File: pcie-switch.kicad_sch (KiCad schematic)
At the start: 130 parts, among them J5 Tag-Connect_TC2050-IDC-NL_2x5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, Q1 BSS138PW,115, Q2 BSS138PW,115, Q3 BSS138PW,115, Q4 BSS138PW,115, Q5 BSS138PW,115, U4 PI7C9X3G606GP, U5 NTS0302JKZ, U6 93AA66C_SOIC

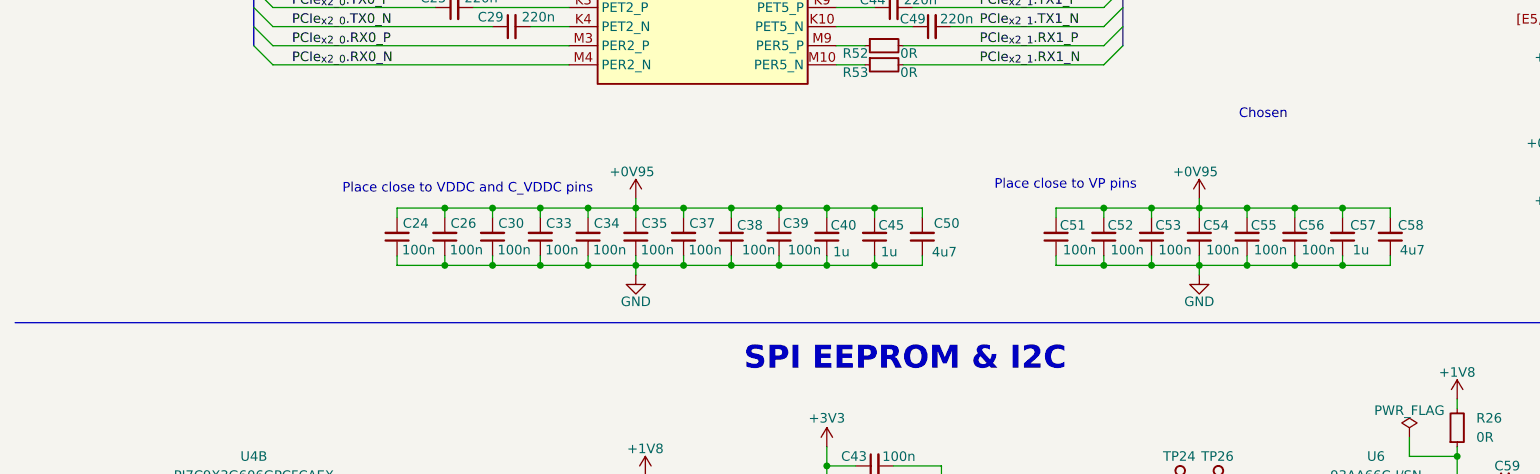
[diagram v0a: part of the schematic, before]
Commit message: [#101557] Add decoupling caps on VDDR, C_VDDR and VPH
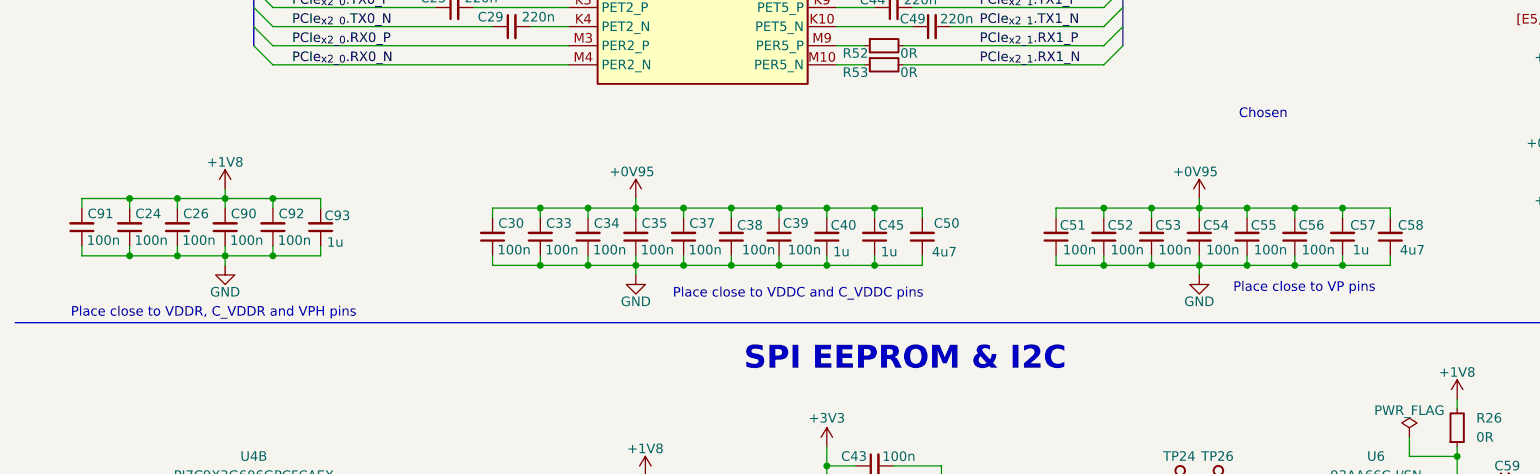
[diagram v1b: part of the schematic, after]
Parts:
- added C90, C91, C92: C_100n_0402, antmicro-footprints:C_0402_1005Metric, symbol antmicroCapacitors0402:C_100n_0402
- added C93: C_1u_0402, antmicro-footprints:C_0402_1005Metric, symbol antmicroCapacitors0402:C_1u_0402
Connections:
- net +0V95: no longer C24.2, C26.2
- net +1V8: now also C24.2, C26.2, C90.2, C91.2, C92.2, C93.2
- net GND: now also C90.1, C91.1, C92.1, C93.1
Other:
- note added: "Place close to VDDR, C_VDDR and VPH pins"
- moved on the sheet: C24, C26

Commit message: [#101557] Change status led to HP_LED4
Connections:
- net at TP37.1: now also U4.H12 (HP_LED6); no longer U4.F12 (HP_LED4)
- net HP_LED6 renamed HP_LED4
- net HP_LED4: now also U4.F12 (HP_LED4); no longer U4.H12 (HP_LED6)
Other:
- moved on the sheet: TP37
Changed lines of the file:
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@@
 	(wire
 		(pts
+			(xy 321.31 59.69) (xy 322.58 59.69)
+		)
+		(stroke
+			(width 0)
+			(type default)
+		)
+	)
+	(wire
+		(pts
 			(xy 217.17 119.38) (xy 222.25 119.38)
 		)
@@
 	(wire
 		(pts
-			(xy 321.31 54.61) (xy 322.58 54.61)
+			(xy 321.31 54.61) (xy 335.28 54.61)
 		)
 		(stroke
@@
 		)
 	)
-	(wire
-		(pts
-			(xy 321.31 59.69) (xy 335.28 59.69)
-		)
-		(stroke
-			(width 0)
-			(type default)
-		)
-	)
 	(bus
 		(pts
@@
 		)
 	)
-	(label "HP_LED6"
+	(label "HP_LED4"
 		(at 44.45 248.92 0)
 		(effects
@@
 		)
 	)
-	(label "HP_LED6"
-		(at 335.28 59.69 180)
+	(label "HP_LED4"
+		(at 335.28 54.61 180)
 		(effects
 			(font
@@
 	(symbol
 		(lib_id "antmicroTestPoints:TP_1mm_SMD")
-		(at 322.58 54.61 0)
+		(at 322.58 59.69 0)
 		(unit 1)
 		(body_style 1)
@@
 		(fields_autoplaced yes)
 		(property "Reference" "TP37"
-			(at 327.66 54.61 0)
+			(at 327.66 59.69 0)
 			(show_name no)
 			(do_not_autoplace no)
@@
 		)
 		(property "Value" "TP_1mm_SMD"
-			(at 337.82 62.23 0)
+			(at 337.82 67.31 0)
 			(hide yes)
 			(show_name no)
@@
 		)
 		(property "Footprint" "antmicro-footprints:TP_SMD_1mm"
-			(at 337.82 64.77 0)
+			(at 337.82 69.85 0)
 			(hide yes)
 			(show_name no)
@@
 		)
 		(property "Datasheet" ""
-			(at 340.36 67.31 0)
+			(at 340.36 72.39 0)
 			(hide yes)
 			(show_name no)
@@
 		)
 		(property "Description" "Test point 1mm SMD"
-			(at 337.82 74.93 0)
+			(at 337.82 80.01 0)
 			(hide yes)
 			(show_name no)
@@
 		)
 		(property "MPN" ""
-			(at 322.58 54.61 0)
+			(at 322.58 59.69 0)
 			(hide yes)
 			(show_name no)
@@
 		)
 		(property "Manufacturer" ""
-			(at 322.58 54.61 0)
+			(at 322.58 59.69 0)
 			(hide yes)
 			(show_name no)
@@
 		)
 		(property "Author" "Antmicro"
-			(at 337.82 69.85 0)
+			(at 337.82 74.93 0)
 			(hide yes)
 			(show_name no)
@@
 		)
 		(property "License" "Apache-2.0"
-			(at 337.82 72.39 0)
+			(at 337.82 77.47 0)
 			(hide yes)
 			(show_name no)

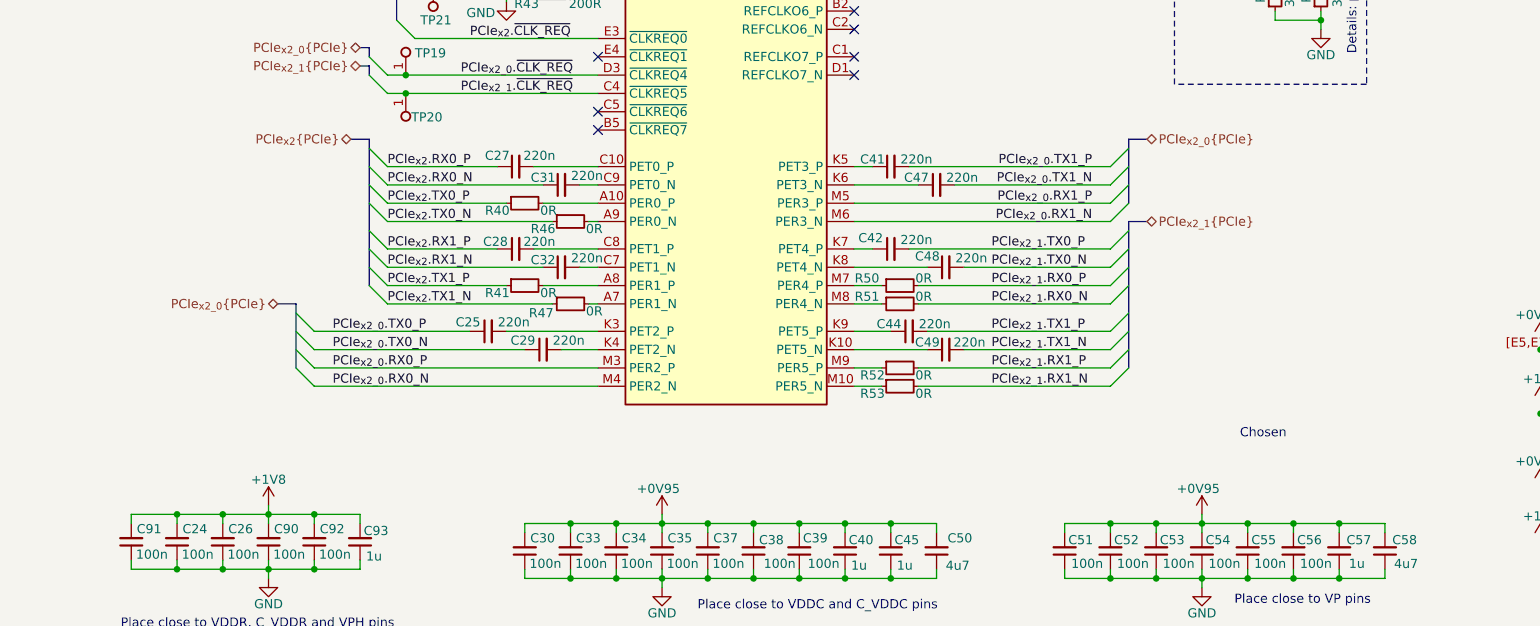
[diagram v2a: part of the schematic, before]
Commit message: [#101557] Add additional labels on HS lines
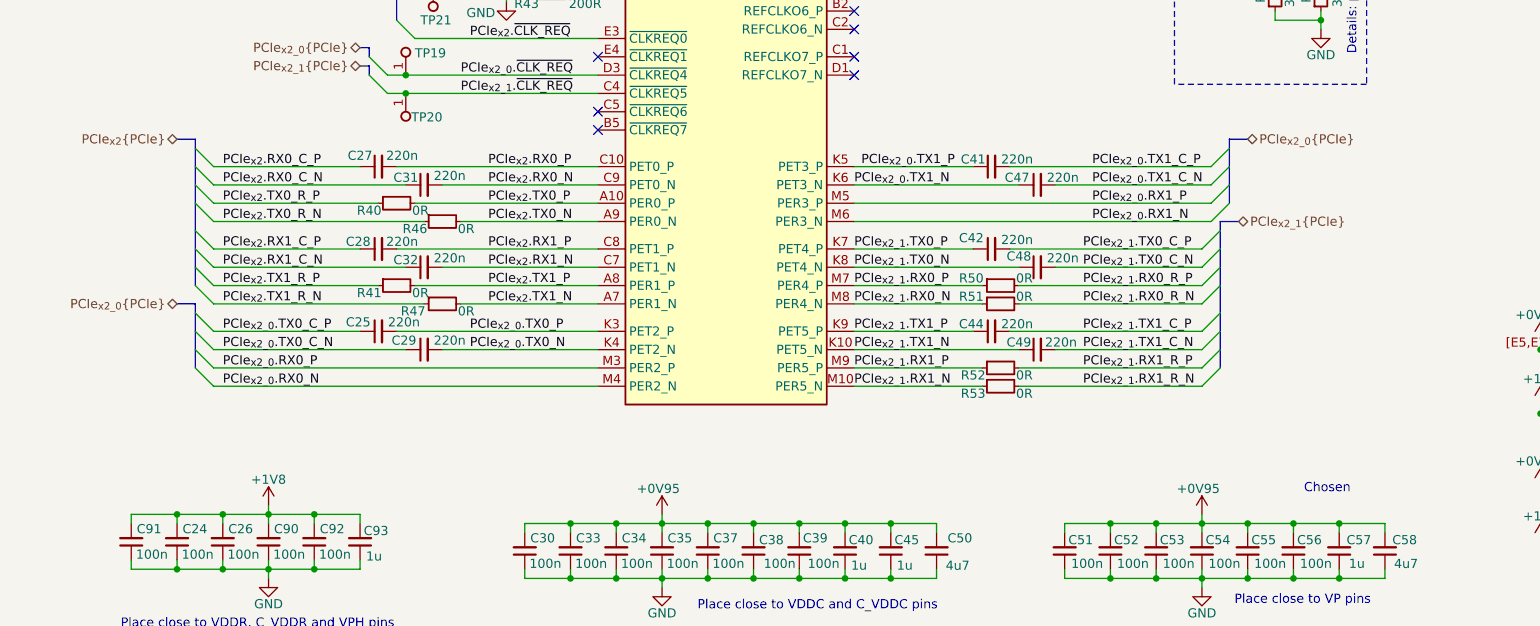
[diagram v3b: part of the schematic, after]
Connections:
- net PCIe_{x2_0}.TX0_N: now also C29.2, U4.K4 (PET2_N); no longer C29.1
- net PCIe_{x2_0}.TX0_P: now also C25.2, U4.K3 (PET2_P); no longer C25.1
- net PCIe_{x2_0}.TX1_N: now also C47.1, U4.K6 (PET3_N); no longer C47.2
- net PCIe_{x2_0}.TX1_P: now also C41.1, U4.K5 (PET3_P); no longer C41.2
- net PCIe_{x2_1}.RX0_N: now also R51.1, U4.M8 (PER4_N); no longer R51.2
- net PCIe_{x2_1}.RX0_P: now also R50.1, U4.M7 (PER4_P); no longer R50.2
- net PCIe_{x2_1}.RX1_N: now also R53.1, U4.M10 (PER5_N); no longer R53.2
- net PCIe_{x2_1}.RX1_P: now also R52.1, U4.M9 (PER5_P); no longer R52.2
- net PCIe_{x2_1}.TX0_N: now also C48.1, U4.K8 (PET4_N); no longer C48.2
- net PCIe_{x2_1}.TX0_P: now also C42.1, U4.K7 (PET4_P); no longer C42.2
- net PCIe_{x2_1}.TX1_N: now also C49.1, U4.K10 (PET5_N); no longer C49.2
- net PCIe_{x2_1}.TX1_P: now also C44.1, U4.K9 (PET5_P); no longer C44.2
- net PCIe_{x2}.RX0_N: now also C31.2, U4.C9 (PET0_N); no longer C31.1
- net PCIe_{x2}.RX0_P: now also C27.2, U4.C10 (PET0_P); no longer C27.1
- net PCIe_{x2}.RX1_N: now also C32.2, U4.C7 (PET1_N); no longer C32.1
- net PCIe_{x2}.RX1_P: now also C28.2, U4.C8 (PET1_P); no longer C28.1
- net PCIe_{x2}.TX0_N: now also R46.2, U4.A9 (PER0_N); no longer R46.1
- net PCIe_{x2}.TX0_P: now also R40.2, U4.A10 (PER0_P); no longer R40.1
- net PCIe_{x2}.TX1_N: now also R47.2, U4.A7 (PER1_N); no longer R47.1
- net PCIe_{x2}.TX1_P: now also R41.2, U4.A8 (PER1_P); no longer R41.1
- new net PCIe_{x2_0}.TX0_C_N: C29.1
- new net PCIe_{x2_0}.TX0_C_P: C25.1
- new net PCIe_{x2_0}.TX1_C_N: C47.2
- new net PCIe_{x2_0}.TX1_C_P: C41.2
- new net PCIe_{x2_1}.RX0_R_N: R51.2
- new net PCIe_{x2_1}.RX0_R_P: R50.2
- new net PCIe_{x2_1}.RX1_R_N: R53.2
- new net PCIe_{x2_1}.RX1_R_P: R52.2
- new net PCIe_{x2_1}.TX0_C_N: C48.2
- new net PCIe_{x2_1}.TX0_C_P: C42.2
- new net PCIe_{x2_1}.TX1_C_N: C49.2
- new net PCIe_{x2_1}.TX1_C_P: C44.2
- new net PCIe_{x2}.RX0_C_N: C31.1
- new net PCIe_{x2}.RX0_C_P: C27.1
- new net PCIe_{x2}.RX1_C_N: C32.1
- new net PCIe_{x2}.RX1_C_P: C28.1
- new net PCIe_{x2}.TX0_R_N: R46.1
- new net PCIe_{x2}.TX0_R_P: R40.1
- new net PCIe_{x2}.TX1_R_N: R47.1
- new net PCIe_{x2}.TX1_R_P: R41.1
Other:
- moved on the sheet: C25, C27, C28, C29, C31, C32, C41, C42, C44, C47, C48, C49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

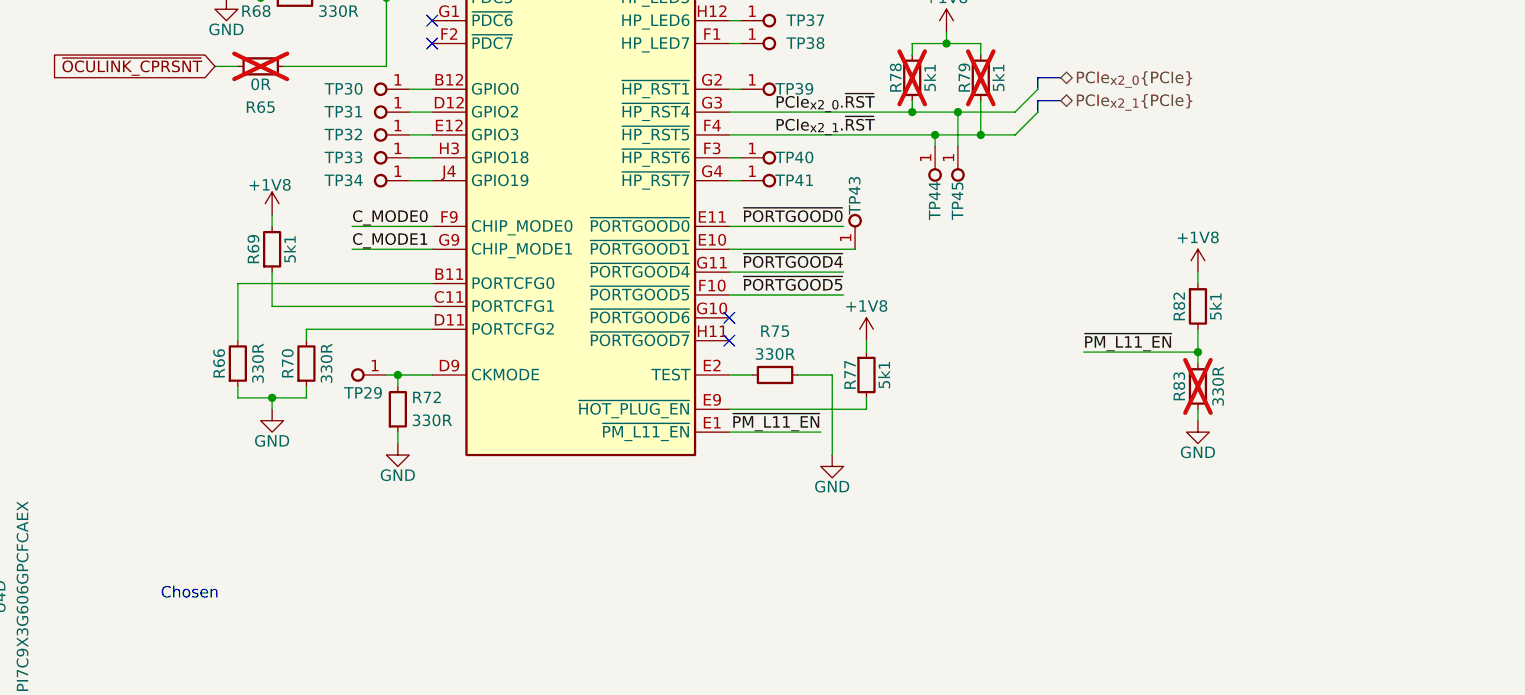
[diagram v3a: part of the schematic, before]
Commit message: [#101859] Prettify silkscreen, mark boostrap signals
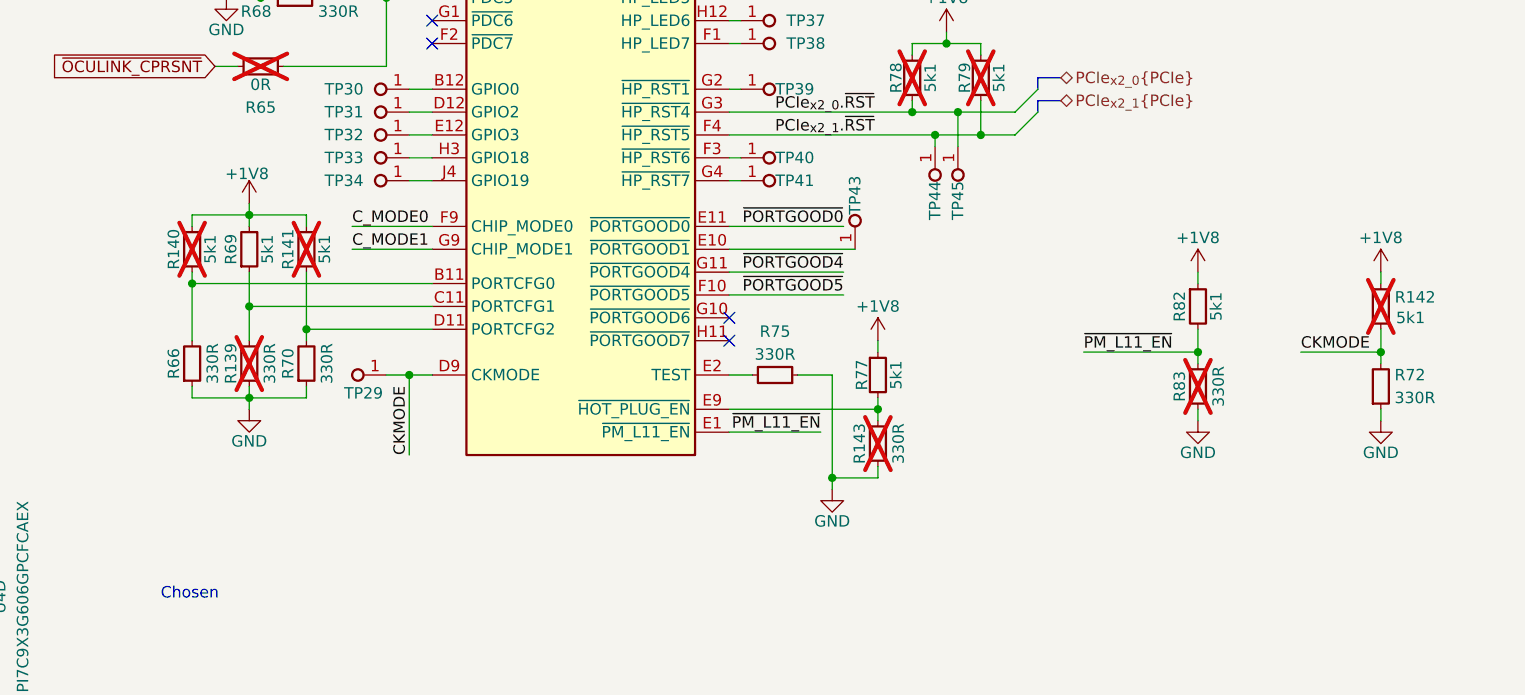
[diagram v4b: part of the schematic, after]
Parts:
- added R139, R143: R_330R_0402, antmicro-footprints:R_0402_1005Metric, symbol antmicroResistors0402:R_330R_0402
- added R140, R141, R142: R_5k1_0402, antmicro-footprints:R_0402_1005Metric, symbol antmicroResistors0402:R_5k1_0402
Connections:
- net +1V8: now also R140.2, R141.2, R142.1
- net GND: now also R139.1, R143.1
- net at R69.1, U4.C11 (PORTCFG1): now also R139.2
- net CKMODE: now reaches R72.2, TP29.1, U4.D9 (CKMODE)
- net CKMODE: now also R142.2
- net at R66.2, U4.B11 (PORTCFG0): now also R140.1
- net at R70.2, U4.D11 (PORTCFG2): now also R141.1
- net at R77.2, U4.E9 (~{HOT_PLUG_EN}): now also R143.2
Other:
- moved on the sheet: R66, R69, R72, R77
